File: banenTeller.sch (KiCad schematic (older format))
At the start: 1 part

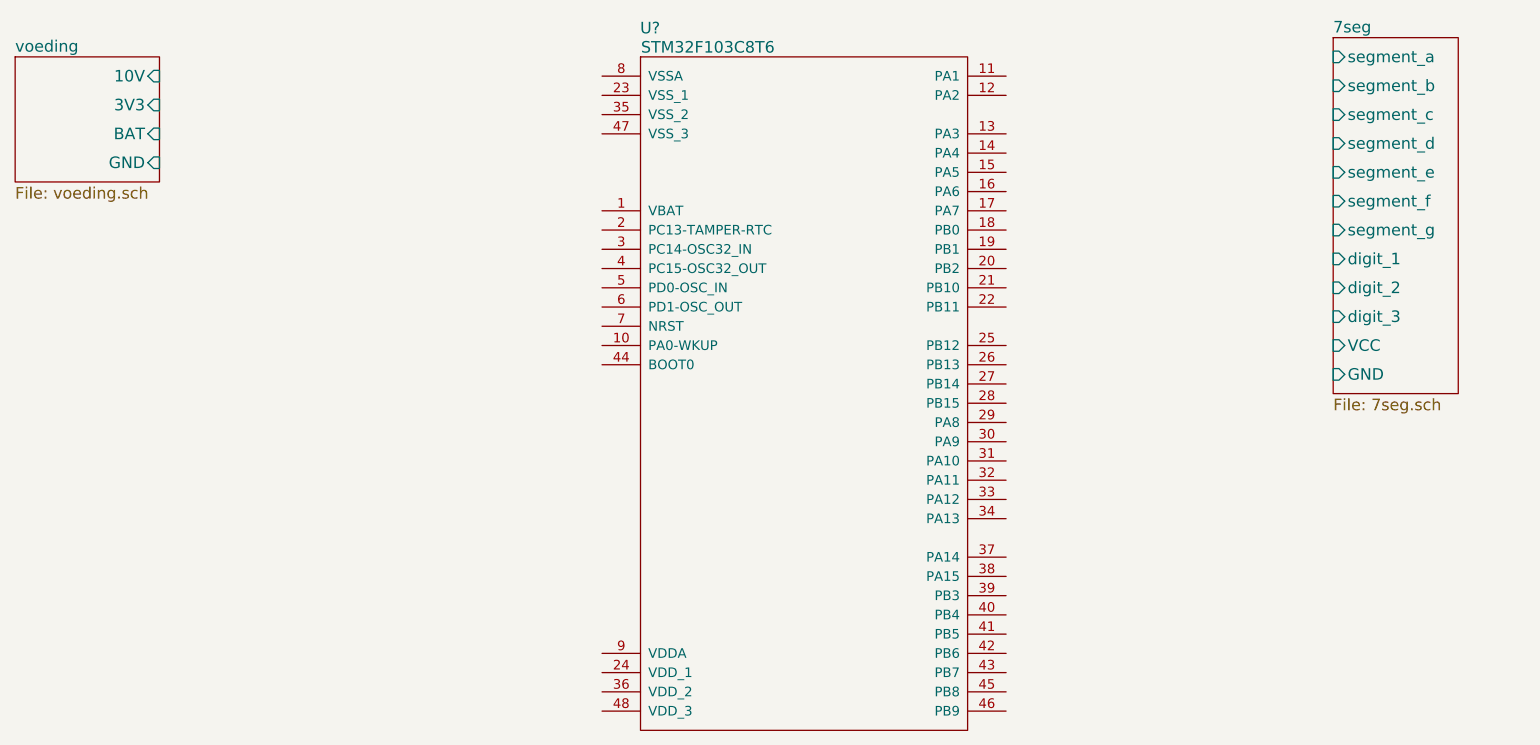
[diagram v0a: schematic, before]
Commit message: added HC-05 symbol
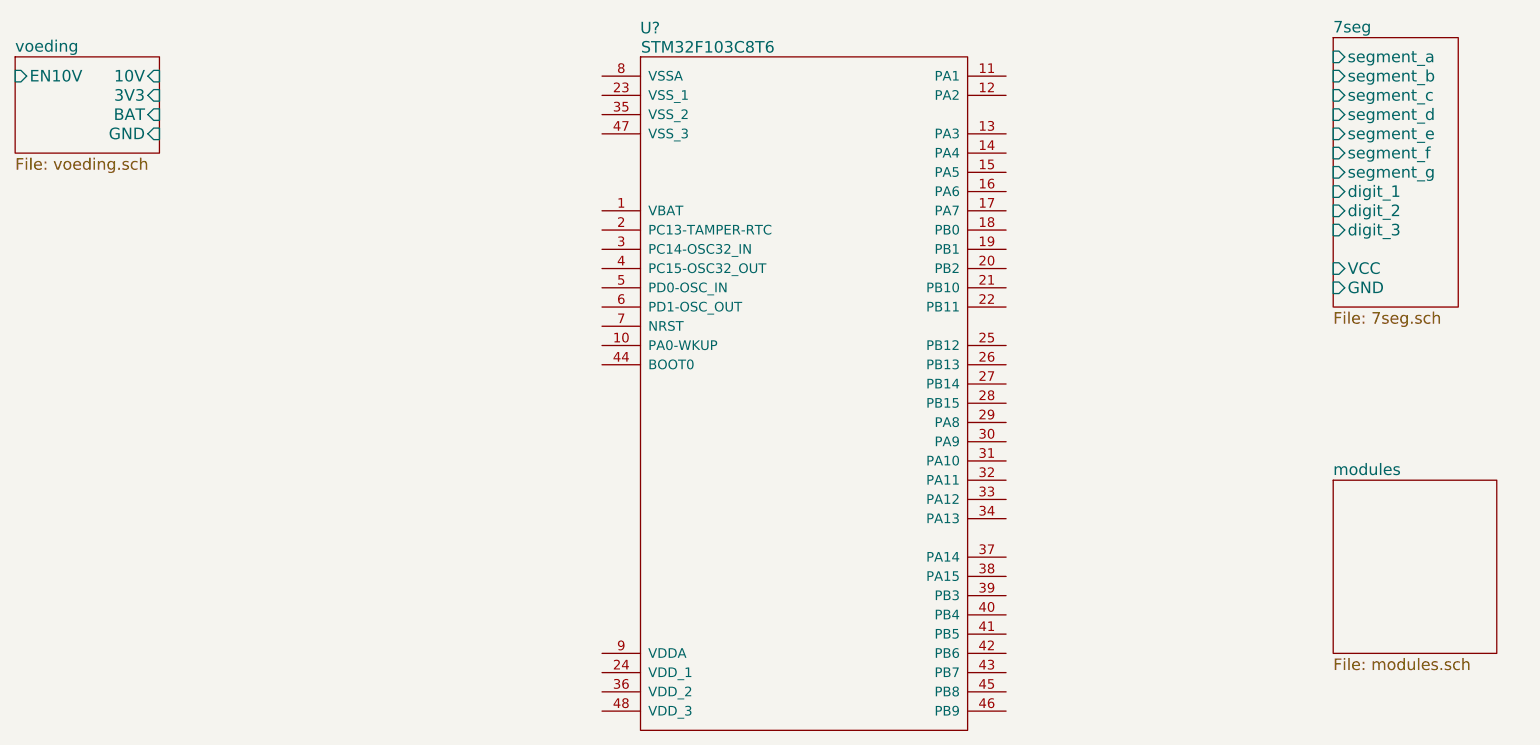
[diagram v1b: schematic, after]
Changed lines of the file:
@@
 $Descr A4 11693 8268
 encoding utf-8
-Sheet 1 3
+Sheet 1 4
 Title ""
 Date ""
@@
 $EndComp
 $Sheet
-S 8100 1200 650  1850
+S 8100 1200 650  1400
 U 5AABD94C
 F0 "7seg" 60
 F1 "7seg.sch" 60
 F2 "segment_a" I L 8100 1300 60
-F3 "segment_b" I L 8100 1450 60
-F4 "segment_c" I L 8100 1600 60
-F5 "segment_d" I L 8100 1750 60
-F6 "segment_e" I L 8100 1900 60
-F7 "segment_f" I L 8100 2050 60
-F8 "segment_g" I L 8100 2200 60
-F9 "digit_1" I L 8100 2350 60
-F10 "digit_2" I L 8100 2500 60
-F11 "digit_3" I L 8100 2650 60
-F12 "VCC" I L 8100 2800 60
-F13 "GND" I L 8100 2950 60
+F3 "segment_b" I L 8100 1400 60
+F4 "segment_c" I L 8100 1500 60
+F5 "segment_d" I L 8100 1600 60
+F6 "segment_e" I L 8100 1700 60
+F7 "segment_f" I L 8100 1800 60
+F8 "segment_g" I L 8100 1900 60
+F9 "digit_1" I L 8100 2000 60
+F10 "digit_2" I L 8100 2100 60
+F11 "digit_3" I L 8100 2200 60
+F12 "VCC" I L 8100 2400 60
+F13 "GND" I L 8100 2500 60
 $EndSheet
 $Sheet
-S 1250 1300 750  650
+S 1250 1300 750  500
 U 5AB8FBF7
 F0 "voeding" 60
 F1 "voeding.sch" 60
-F2 "BAT" I R 2000 1700 60
-F3 "GND" I R 2000 1850 60
-F4 "3V3" I R 2000 1550 60
+F2 "BAT" I R 2000 1600 60
+F3 "GND" I R 2000 1700 60
+F4 "3V3" I R 2000 1500 60
 F5 "10V" I R 2000 1400 60
+F6 "EN10V" I L 1250 1400 60
+$EndSheet
+$Sheet
+S 8100 3500 850  900
+U 5AC2590A
+F0 "modules" 60
+F1 "modules.sch" 60
 $EndSheet
 $EndSCHEMATC
